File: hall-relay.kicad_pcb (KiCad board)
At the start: 2 copper layers, 37.5 x 11.7 mm, 16 parts, among them J1 Screw_Terminal_1x04, Q1 AO3400, U1 HT71xx, U2 Hall-A3212

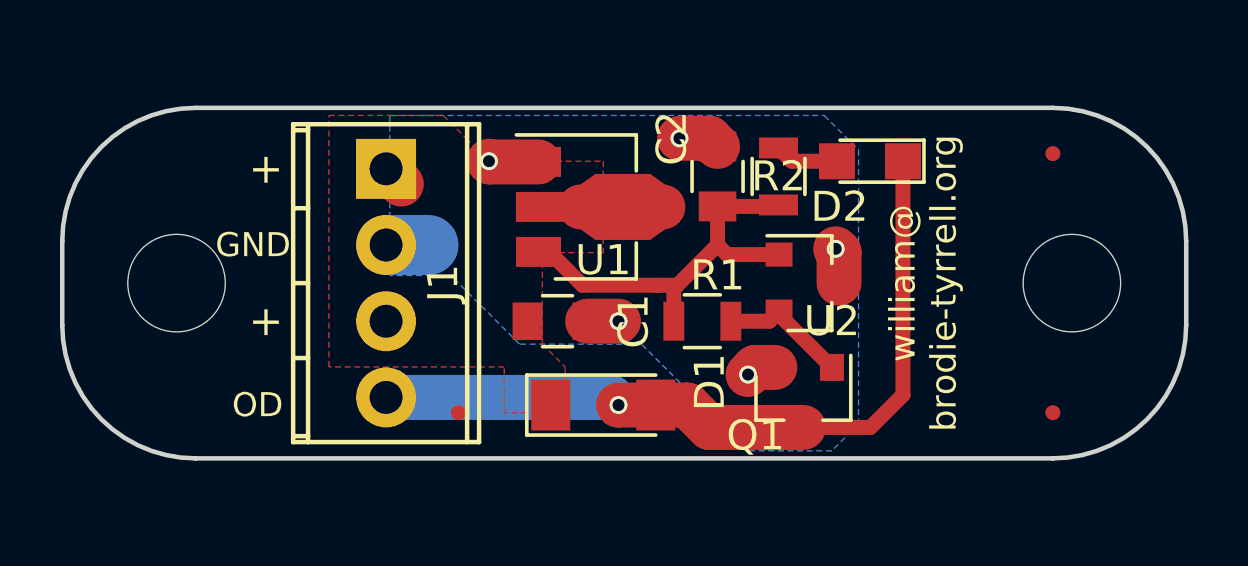
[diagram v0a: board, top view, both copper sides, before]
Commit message: added LED pullup option to unregulated; avoids LED reverse-breakdown problems
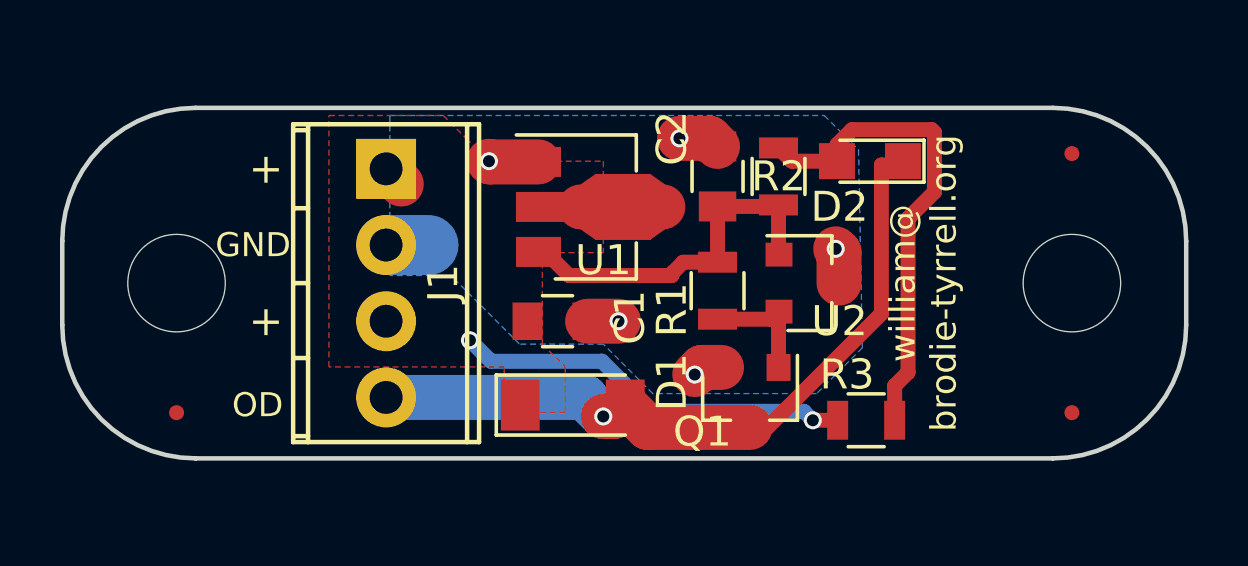
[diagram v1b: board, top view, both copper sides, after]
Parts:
- added R3: 12k, Resistors_SMD:R_0805, F.Cu at (142.4, 85.3)
- moved ? 9.40 mm to (119.4, 85.1)
- moved Q1 1.78 mm to (138.5, 84.6)
- moved R1 1.14 mm to (137.4, 81.0), turned to 270 degrees
- moved D1 1.02 mm to (132.6, 84.8)
- moved ? 0.63 mm to (149.2, 85.1)
- moved ? 0.63 mm to (149.2, 76.5)
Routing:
- net Net-(D2-Pad2): track 2.13 -> 16.3 mm
- net /12V: track 3.46 -> 16.8 mm, vias 0 -> 2
- net /OD: track 25.9 -> 24.6 mm
- net Net-(C2-Pad1): track 13.7 -> 12.4 mm

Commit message: shortened board to fit panelisation
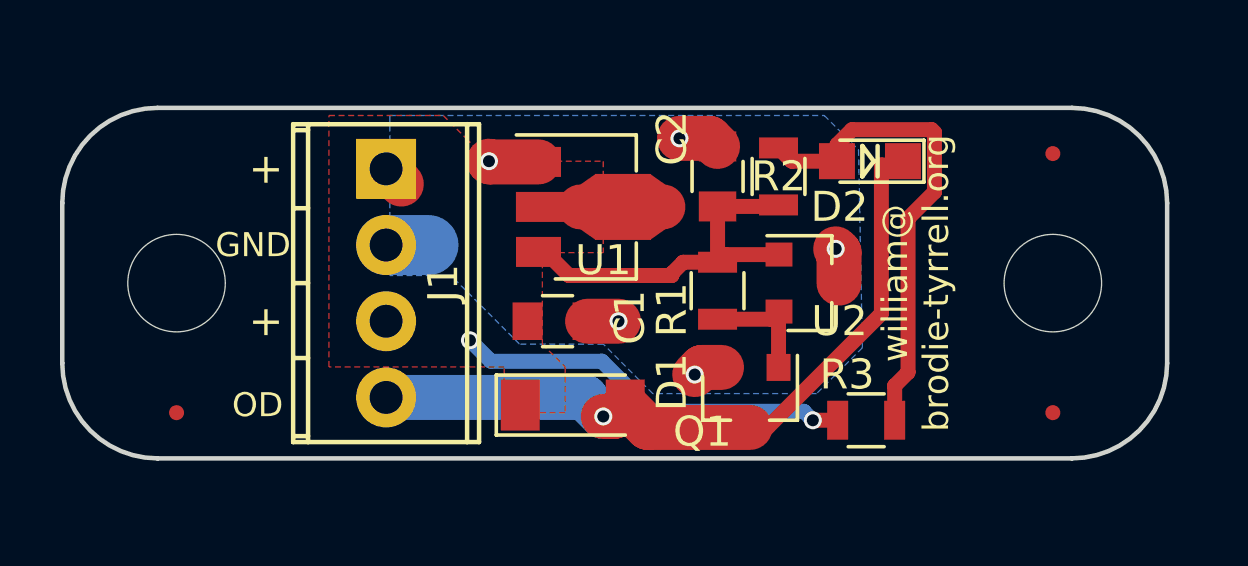
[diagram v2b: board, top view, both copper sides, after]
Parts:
- moved ? 0.63 mm to (148.6, 85.1)
- moved ? 0.63 mm to (148.6, 76.5)
- moved REF** 0.63 mm to (148.6, 80.8)
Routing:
- net Net-(C2-Pad1): track 12.4 -> 13.0 mm
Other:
- board size 37.5 x 11.7 mm -> 36.8 x 11.7 mm
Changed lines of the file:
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@@
     (area 113.711738 66.345809 153.925 93.698191)
     (thickness 1)
-    (drawings 14)
-    (tracks 69)
+    (drawings 18)
+    (tracks 70)
     (zones 0)
     (modules 17)
@@
     (43 Eco2.User user)
     (44 Edge.Cuts user)
-    (45 Margin user)
+    (45 Margin user hide)
     (46 B.CrtYd user)
     (47 F.CrtYd user)
@@
     (zone_45_only no)
     (trace_min 0.2)
-    (segment_width 1)
+    (segment_width 0.15)
     (edge_width 0.15)
     (via_size 0.6)
@@
   )
   (module smd:FID0.5 (layer F.Cu)
-    (at 149.225 85.09)
+    (at 148.59 85.09)
     (tags "fid, fiducial")
     (fp_text reference "" (at 0.5 2) (layer F.SilkS)
@@
   )
   (module pcb:hole3mm (layer F.Cu)
-    (at 149.225 80.772)
+    (at 148.59 80.772)
     (fp_text reference REF** (at 0 0.5) (layer F.SilkS) hide
       (effects (font (size 1 1) (thickness 0.15)))
@@
   )
   (module smd:FID0.5 (layer F.Cu)
-    (at 149.225 76.454)
+    (at 148.59 76.454)
     (tags "fid, fiducial")
     (fp_text reference "" (at 0.5 2) (layer F.SilkS)
@@
     )
   )
+  (gr_line (start 142.748 77.216) (end 142.748 76.2) (layer F.SilkS) (width 0.15))
+  (gr_line (start 142.24 76.2) (end 142.24 77.216) (layer F.SilkS) (width 0.15))
+  (gr_line (start 142.621 76.708) (end 142.24 76.2) (layer F.SilkS) (width 0.15))
+  (gr_line (start 142.621 76.708) (end 142.24 77.216) (layer F.SilkS) (width 0.15))
   (gr_text "Hall Relay NC\nRev.A 201712\ngithub.com/\nphenidone" (at 131.826 80.772 90) (layer B.SilkS)
     (effects (font (size 1 1) (thickness 0.2)) (justify mirror))
   )
-  (gr_text "william@\nbrodie-tyrrell.org" (at 144.272 80.772 90) (layer F.SilkS)
+  (gr_text "william@\nbrodie-tyrrell.org" (at 144.018 80.772 90) (layer F.SilkS)
     (effects (font (size 0.85 0.85) (thickness 0.15)))
   )
@@
     (effects (font (size 1 1) (thickness 0.2)) (justify right))
   )
-  (gr_line (start 115.57 82.169) (end 115.57 79.375) (layer Edge.Cuts) (width 0.15))
-  (gr_arc (start 148.59 82.169) (end 153.035 82.169) (angle 90) (layer Edge.Cuts) (width 0.15))
-  (gr_arc (start 148.59 79.375) (end 148.59 74.93) (angle 90) (layer Edge.Cuts) (width 0.15))
-  (gr_arc (start 120.015 79.375) (end 115.57 79.375) (angle 90) (layer Edge.Cuts) (width 0.15))
-  (gr_arc (start 120.015 82.169) (end 120.015 86.614) (angle 90) (layer Edge.Cuts) (width 0.15))
-  (gr_line (start 148.59 74.93) (end 120.015 74.93) (layer Edge.Cuts) (width 0.15))
-  (gr_line (start 153.035 79.375) (end 153.035 82.169) (layer Edge.Cuts) (width 0.15))
-  (gr_line (start 120.015 86.614) (end 148.59 86.614) (layer Edge.Cuts) (width 0.15))
+  (gr_line (start 115.57 83.439) (end 115.57 78.105) (layer Edge.Cuts) (width 0.15))
+  (gr_arc (start 149.225 83.439) (end 152.4 83.439) (angle 90) (layer Edge.Cuts) (width 0.15))
+  (gr_arc (start 149.225 78.105) (end 149.225 74.93) (angle 90) (layer Edge.Cuts) (width 0.15))
+  (gr_arc (start 118.745 78.105) (end 115.57 78.105) (angle 90) (layer Edge.Cuts) (width 0.15))
+  (gr_arc (start 118.745 83.439) (end 118.745 86.614) (angle 90) (layer Edge.Cuts) (width 0.15))
+  (gr_line (start 149.225 74.93) (end 118.745 74.93) (layer Edge.Cuts) (width 0.15))
+  (gr_line (start 152.4 78.105) (end 152.4 83.439) (layer Edge.Cuts) (width 0.15))
+  (gr_line (start 118.745 86.614) (end 149.225 86.614) (layer Edge.Cuts) (width 0.15))
   (segment (start 140.589 85.344) (end 140.289001 85.044001) (width 0.5) (layer B.Cu) (net 1))
   (segment (start 129.855557 83.373557) (end 129.159 82.677) (width 0.5) (layer B.Cu) (net 1))
@@
   (via (at 134.112 82.042) (size 0.6) (drill 0.4) (layers F.Cu B.Cu) (net 2))
   (segment (start 126.365 79.502) (end 127.778492 79.502) (width 2) (layer B.Cu) (net 2))
-  (segment (start 139.446 78.166) (end 139.446 79.806) (width 0.5) (layer F.Cu) (net 3))
+  (segment (start 139.462 79.822) (end 137.668 79.822) (width 0.5) (layer F.Cu) (net 3))
+  (segment (start 137.668 79.822) (end 137.414 80.076) (width 0.5) (layer F.Cu) (net 3))
   (segment (start 139.446 79.806) (end 139.462 79.822) (width 0.5) (layer F.Cu) (net 3))
   (segment (start 137.414 80.076) (end 137.414 78.216) (width 0.5) (layer F.Cu) (net 3))
